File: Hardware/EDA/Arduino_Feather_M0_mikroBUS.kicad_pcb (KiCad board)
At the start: 4 copper layers, 38.1 x 69.8 mm, 30 parts, among them J1 HEADER_F_2.54MM_1R8P_ST_AU_PTH, J2 HEADER_F_2.54MM_1R8P_ST_AU_PTH, J3 HEADER_F_2.54MM_1R11P_ST_AU_P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, J4 HEADER_F_2.54MM_1R11P_ST_AU_P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, J5 Molex_0475710001, M1 FID, M2 FID, M3 FID, P1 HEADER_M_2.54MM_1R4P_ST_AU_PTH, P2 HEADER_M_2.54MM_1R4P_ST_AU_PTH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

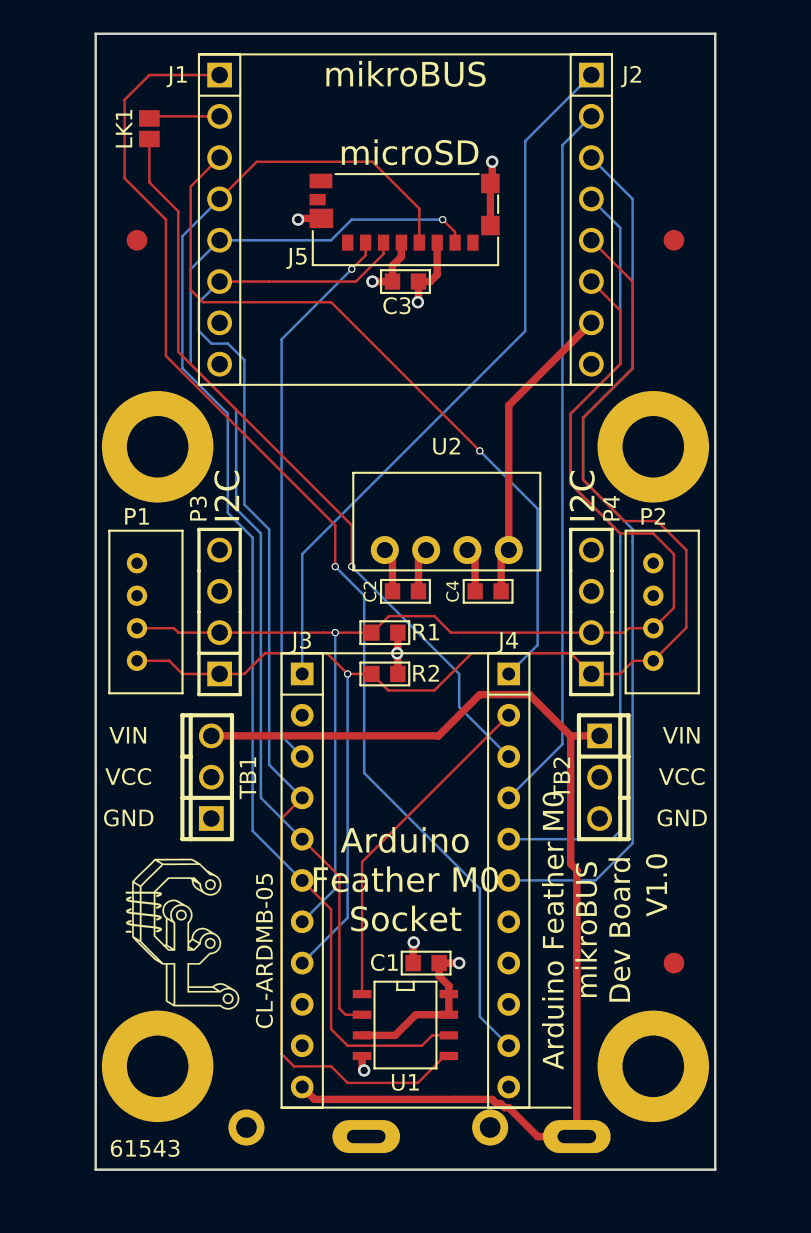
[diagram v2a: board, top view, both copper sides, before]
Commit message: Updated schematic with pin assignments of feather M0 and 5V DC-DC boost power supply.  Updated PCB with feather M0 headers and all routing complete. Few tweaks remain per notes on layout.
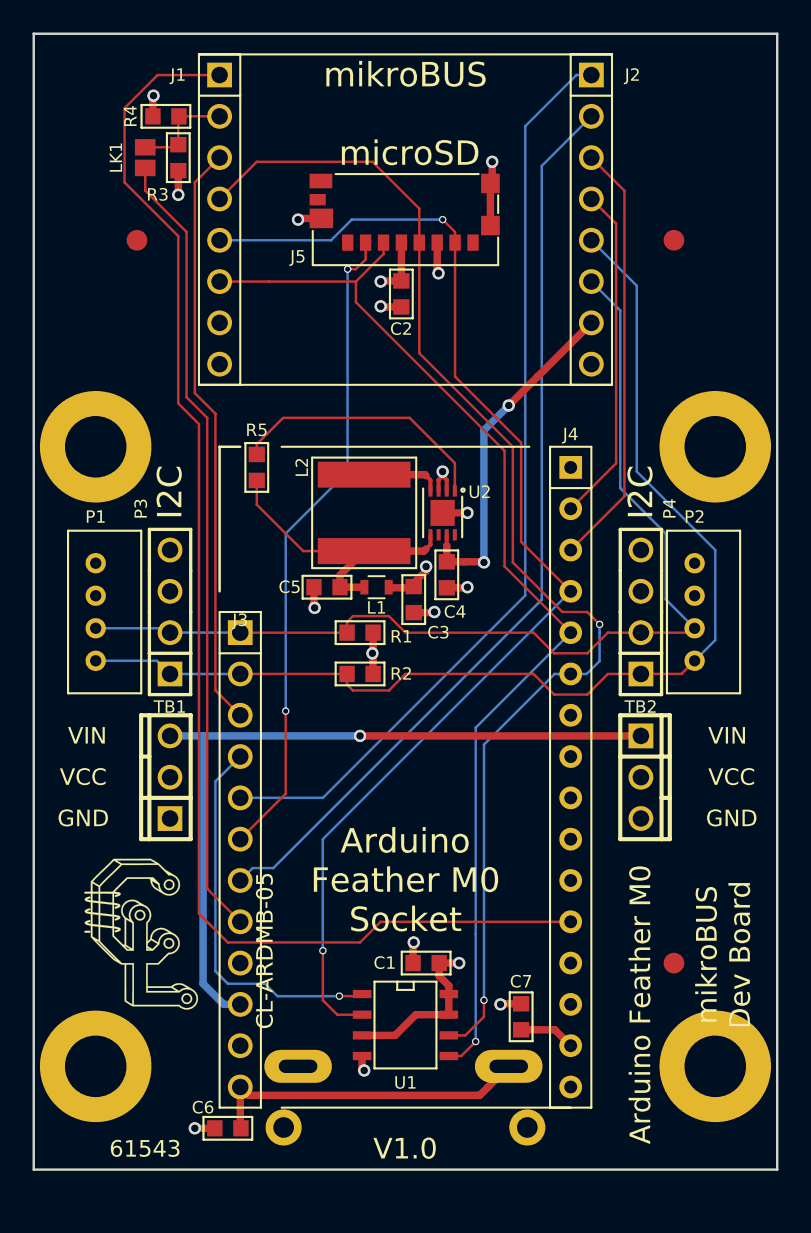
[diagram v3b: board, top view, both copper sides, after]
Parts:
- added C5: 10uF, Passive:0603, F.Cu at (75.2, 65.8)
- added C6: 10uF, Passive:0603, F.Cu at (69.1, 99.1)
- added C7: 0.1uF, Passive:0603, F.Cu at (87.1, 92.2)
- added L1: F_Bead, Passive:L_0603, F.Cu at (78.2, 65.8)
- added L2: 4.7uH, Passive:DG6050C, F.Cu at (77.5, 61.2)
- added R3: DNP, Passive:R0603, F.Cu at (66.0, 39.4)
- added R4: DNP, Passive:R0603, F.Cu at (65.3, 36.8)
- added R5: 4.7k, Passive:R0603, F.Cu at (70.9, 58.4)
- C1, C2, C3: value 1uF -> 0.1uF
- C4: value 1uF -> 10uF
- J3: value HEADER_F_2.54MM_1R11P_ST_AU_PTH -> HEADER_F_2.54MM_1R12P_ST_AU_PTH; footprint Header:HEADER_F_2.54MM_1R11P_ST_AU_PTH -> Header:HEADER_F_2.54MM_1R12P_ST_AU_PTH
- J4: value HEADER_F_2.54MM_1R11P_ST_AU_PTH -> HEADER_F_2.54MM_1R16P_ST_AU_PTH; footprint Header:HEADER_F_2.54MM_1R11P_ST_AU_PTH -> Header:HEADER_F_2.54MM_1R16P_ST_AU_PTH
- U2: value Recom_DC_DC_Conv -> DIO6605B; footprint Power_Supply:Recom_ROE-3.305S -> Active:DFN2-3-8
- moved C3 19.6 mm to (80.5, 66.5), turned to 270 degrees
- moved C2 18.3 mm to (79.8, 47.8), turned to 270 degrees
- moved J4 7.41 mm to (90.2, 77.5)
- moved B1 6.02 mm to (79.9, 95.2)
- moved J3 4.02 mm to (69.8, 82.5)
- moved MH2 3.81 mm to (99.1, 57.1)
- moved MH4 3.81 mm to (99.1, 95.2)
- moved MH1 3.81 mm to (61.0, 57.1)
- moved MH3 3.81 mm to (61.0, 95.2)
- moved P3 3.05 mm to (65.5, 67.3)
- moved P4 3.05 mm to (94.5, 67.3)
- moved C4 2.74 mm to (82.5, 65.0), turned to 270 degrees
- moved P2 2.54 mm to (97.8, 67.3)
- moved TB1 2.54 mm to (65.5, 77.5)
- moved TB2 2.54 mm to (94.5, 77.5)
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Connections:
- net mikroBUS_RST renamed Net-(J1-Pad2)
- B1 pad 1: VIN -> VBAT
- B2 pad 1: 3V3 -> +3V3
- C1 pad 1: 3V3 -> +3V3
- C2 pad 1: 3V3 -> +3V3
- C3 pad 1: 3V3 -> +3V3
- J1 pad 7: 3V3 -> +3V3
- J2 pad 1: D8 -> D9
- J2 pad 2: D2 -> D11
- J3 pad 1: D8 -> SDA
- J3 pad 10: GND -> VIN
- J3 pad 11: VIN -> Net-(J3-Pad11)
- J3 pad 2: (no net) -> SCL
- J3 pad 3: D10 -> D5
- J3 pad 4: MOSI -> D6
- J3 pad 5: MISO -> D9
- J3 pad 6: SCK -> D10
- J3 pad 7: SDA -> D11
- J3 pad 8: SCL -> D12
- J3 pad 9: 3V3 -> D13
- J4 pad 1: D5 -> GND
- J4 pad 10: A0 -> A2
- J4 pad 11: GND -> A1
- J4 pad 2: D4 -> TXD
- J4 pad 3: D3 -> RXD
- J4 pad 4: D2 -> MISO
- J4 pad 5: TXD -> MOSI
- J4 pad 6: RXD -> SCK
- J4 pad 7: (no net) -> A5
- J4 pad 8: (no net) -> A4
- J4 pad 9: (no net) -> A3
- J5 pad 1: (no net) -> Net-(J5-Pad1)
- J5 pad 12: (no net) -> Net-(J5-Pad12)
- J5 pad 13: (no net) -> Net-(J5-Pad13)
- J5 pad 4: 3V3 -> +3V3
- J5 pad 8: (no net) -> Net-(J5-Pad8)
- LK1 pad 1: D3 -> D12
- M1 pad ~: (no net) -> Net-(M1-Pad~)
- M2 pad ~: (no net) -> Net-(M2-Pad~)
- M3 pad ~: (no net) -> Net-(M3-Pad~)
- P1 pad 3: 3V3 -> +3V3
- P2 pad 3: 3V3 -> +3V3
- P3 pad 3: 3V3 -> +3V3
- P4 pad 3: 3V3 -> +3V3
- R1 pad 1: 3V3 -> +3V3
- R2 pad 1: 3V3 -> +3V3
- TB1 pad 2: 3V3 -> +3V3
- TB2 pad 2: 3V3 -> +3V3
- U1 pad 1: D4 -> D6
- U1 pad 3: 3V3 -> +3V3
- U1 pad 7: 3V3 -> +3V3
- U1 pad 8: 3V3 -> +3V3
- U2 pad 1: GND -> Net-(R5-Pad1)
- U2 pad 2: 3V3 -> GND
- U2 pad 4: 5.0V -> /DIO_SW
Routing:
- net D9: track 0.00 -> 56.9 mm
- net D11: track 0.00 -> 56.7 mm
- net D12: track 0.00 -> 48.8 mm
- net D3: track 47.1 -> 0.00 mm, vias 1 -> 0
- net D8: track 44.2 -> 0.00 mm
- net D2: track 44.0 -> 0.00 mm
- net TXD: track 49.2 -> 20.8 mm
- net RXD: track 54.3 -> 26.3 mm
- net +3V3: track 0.00 -> 24.8 mm, vias 0 -> 5
- net D6: track 0.00 -> 23.5 mm, vias 0 -> 1
- net VIN: track 68.9 -> 47.0 mm, vias 0 -> 1
- net D4: track 20.9 -> 0.00 mm
- net VBAT: track 0.00 -> 20.0 mm
- net 3V3: track 19.7 -> 0.00 mm, vias 3 -> 0
- net /DIO_VIN: track 0.00 -> 18.5 mm
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- added copper zone on Power.Cu, net +3V3
- removed copper zone on Power.Cu, net 3V3
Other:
- board size 38.1 x 69.8 mm -> 45.7 x 69.8 mm
- board text added: "NOTES: - Need to add additional 0.050", minimum, between mikroBUS socket and feather (0.100" would be better). - Need to double check component locations of P1, P2, P3, and P4 for consistency across mikroBUS Dev boards - Need to updated 1x16-pin header step file - Need to verify all components have good step files for assembly model - Need to verify inductor and output capacitor sizing for 5V boo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"

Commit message: Updated footprints for B1 and B2. Shifted headers for feather M0 down to allow more room for feather M0 near mikroBUS socket.
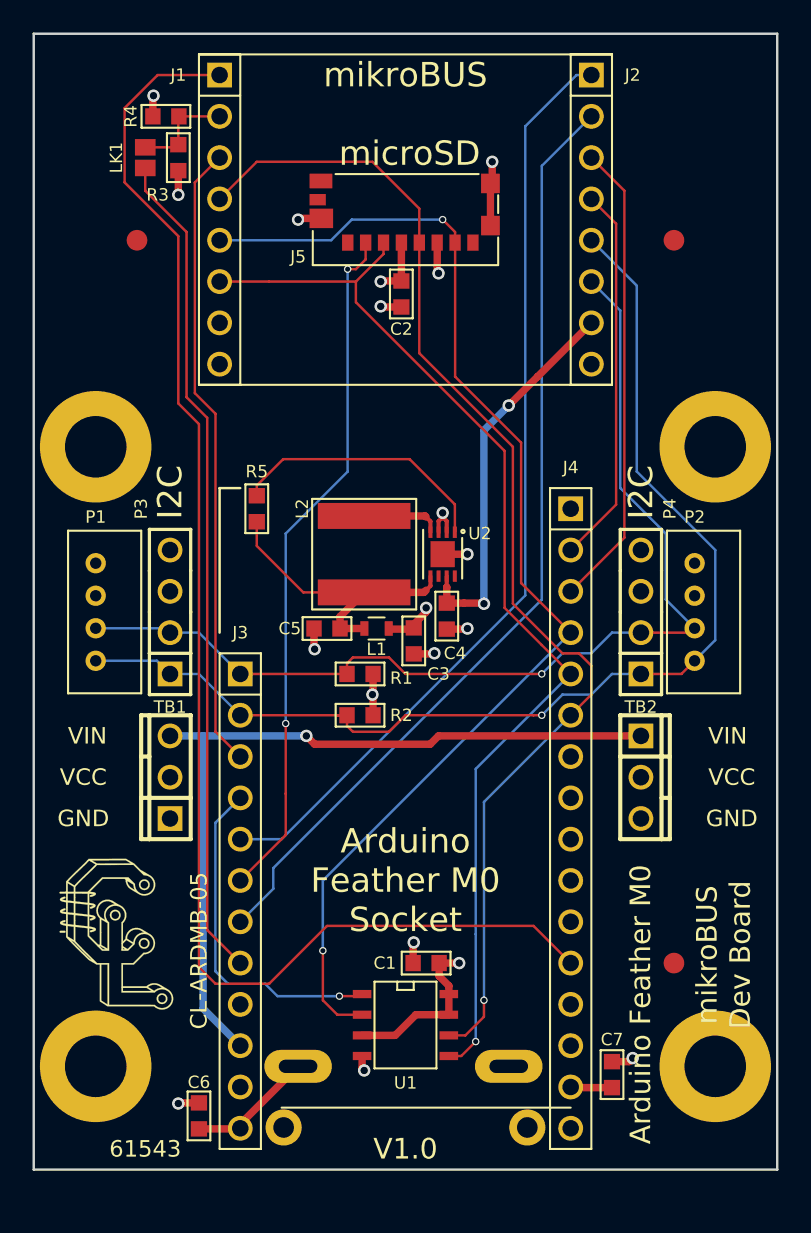
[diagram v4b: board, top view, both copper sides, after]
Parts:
- J4: value HEADER_F_2.54MM_1R16P_ST_AU_PTH -> Val**
- moved C7 6.62 mm to (92.7, 95.8)
- moved J3 2.54 mm to (69.8, 85.1)
- moved J4 2.54 mm to (90.2, 80.0)
- moved R1 2.54 mm to (77.2, 71.1)
- moved L2 2.54 mm to (77.5, 63.8)
- moved R5 2.54 mm to (70.9, 61.0)
- moved U2 2.54 mm to (82.3, 63.8)
- moved C3 2.54 mm to (80.5, 69.1)
- moved C4 2.54 mm to (82.5, 67.6)
- moved C5 2.54 mm to (75.2, 68.3)
- moved L1 2.54 mm to (78.2, 68.3)
- moved R2 2.54 mm to (77.2, 73.7)
- moved C6 1.93 mm to (67.3, 98.3), turned to 90 degrees
- moved G1 1.52 mm to (62.2, 87.1)
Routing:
- net VBAT: track 20.0 -> 7.84 mm
- net A0: track 82.2 -> 87.1 mm
- net RXD: track 26.3 -> 28.9 mm
- net 5.0V: track 21.4 -> 24.0 mm
- net TXD: track 20.8 -> 23.4 mm
- net D5: track 36.1 -> 38.6 mm
- net D12: track 48.8 -> 51.3 mm
- net D6: track 23.5 -> 21.0 mm
- net D10: track 40.2 -> 42.7 mm
- net VIN: track 47.0 -> 49.4 mm
- net SCK: track 76.3 -> 74.5 mm, vias 2 -> 1
- net D11: track 56.7 -> 58.5 mm
- net SCL: track 69.3 -> 71.0 mm, vias 0 -> 1
- net SDA: track 63.3 -> 64.3 mm, vias 0 -> 1
- net D9: track 56.9 -> 58.0 mm
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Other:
- board text added: "NOTES: - Need to add additional 0.050", minimum, between mikroBUS socket and feather (0.100" would be better). - Need to double check component locations of P1, P2, P3, and P4 for consistency across mikroBUS Dev boards - Need to update 1x16-pin header step file - Need to verify all components have good step files for assembly model - Need to verify inductor and output capacitor sizing for 5V boos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"
- board text removed: "NOTES: - Need to add additional 0.050", minimum, between mikroBUS socket and feather (0.100" would be better). - Need to double check component locations of P1, P2, P3, and P4 for consistency across mikroBUS Dev boards - Need to updated 1x16-pin header step file - Need to verify all components have good step files for assembly model - Need to verify inductor and output capacitor sizing for 5V boo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"
